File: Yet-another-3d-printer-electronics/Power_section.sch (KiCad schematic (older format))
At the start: 33 parts, among them U7 AOZ1284PI, U8 AOZ1284PI

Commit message: Replace aoz1284pi by AP1501
Signed-off-by: Mateusz Krawczuk <mat.krawczuk@gmail.com>
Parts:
- removed C17, C18, C19, C20, C21, C22, C? (x3): C, symbol C
- removed D43, D44, D?: D_Schottky, symbol D_Schottky
- removed L2, L3, L?: INDUCTOR, symbol INDUCTOR
- removed R24, R25, R26, R27, R28, R29, R? (x6), RC1, RC2, RC?: R, symbol R
- removed U7, U8, U?: AOZ1284PI, symbol AOZ1284PI
- added C? (x6): CP, symbol CP
- added D? (x3): D_Schottky, symbol D_Schottky
- added L? (x3): L, symbol L
- added R? (x6): R, symbol R
- added U? (x3): AP1501, symbol AP1501
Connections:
- wire segments 81 -> 48

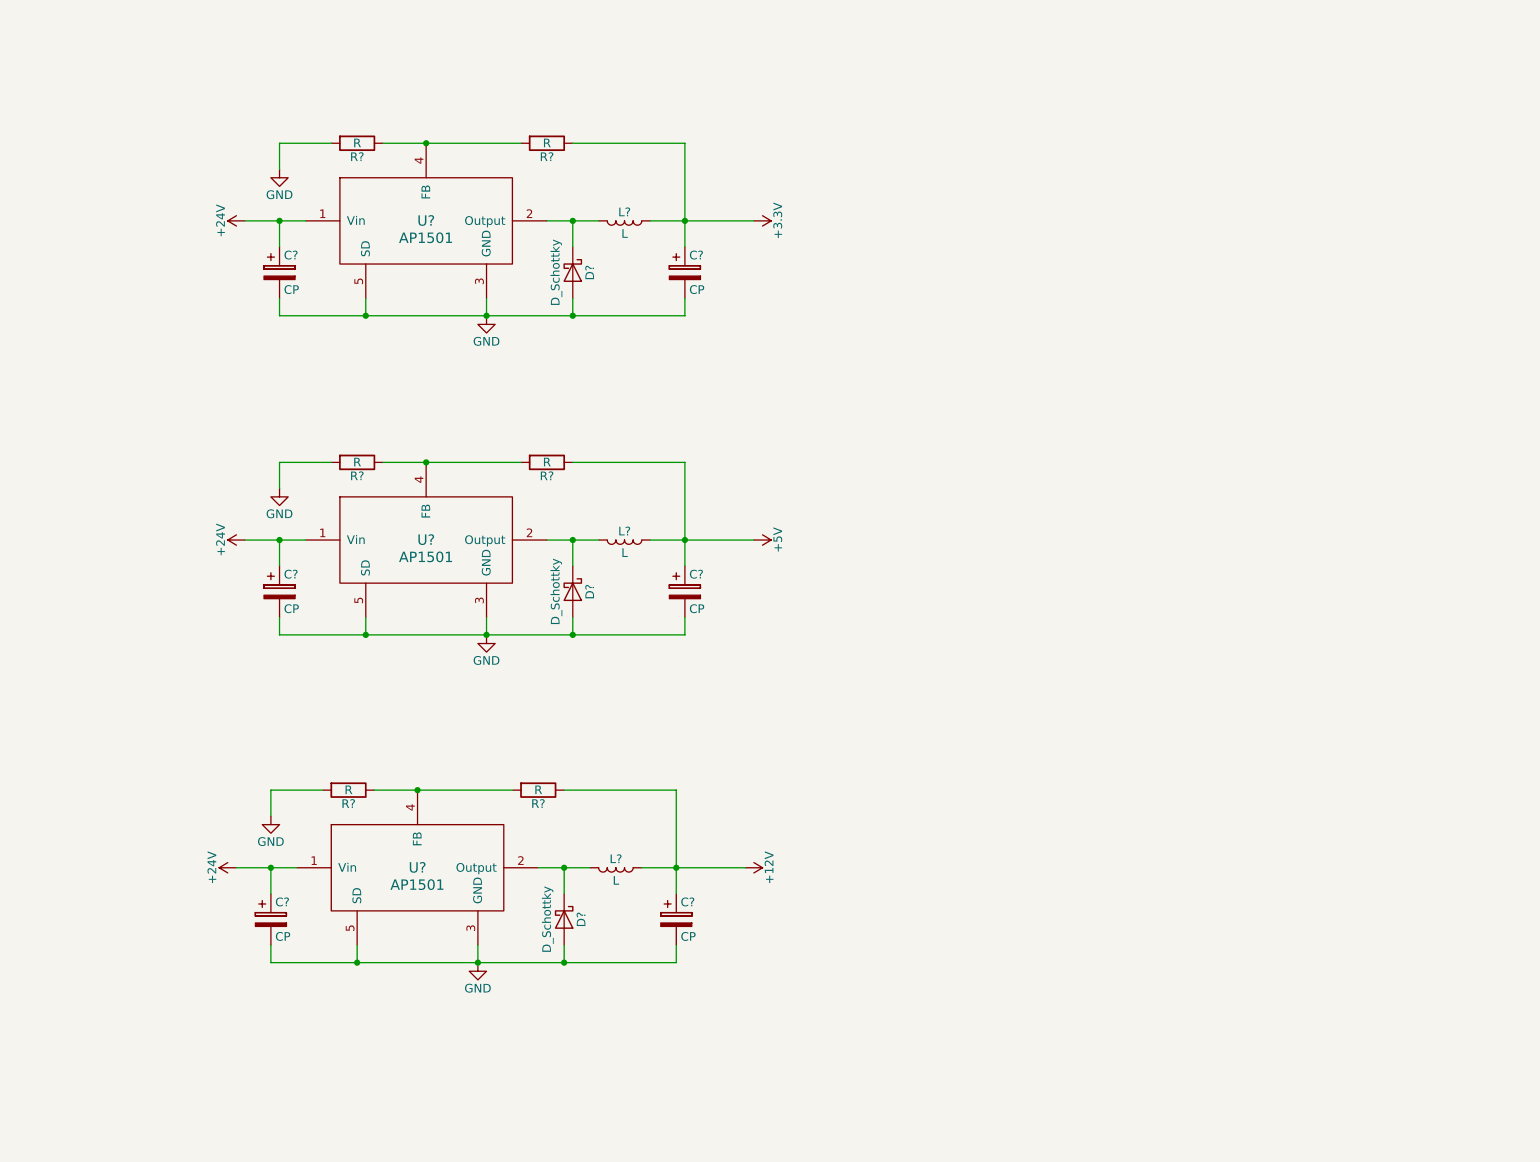
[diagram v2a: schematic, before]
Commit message: Add additional stepstick, hotend fan and heater and temperature sensor
Extruder stepsticks have independ enables pins. Vcc was replace by valid
power source.

Signed-off-by: Mateusz Krawczuk <mat.krawczuk@gmail.com>
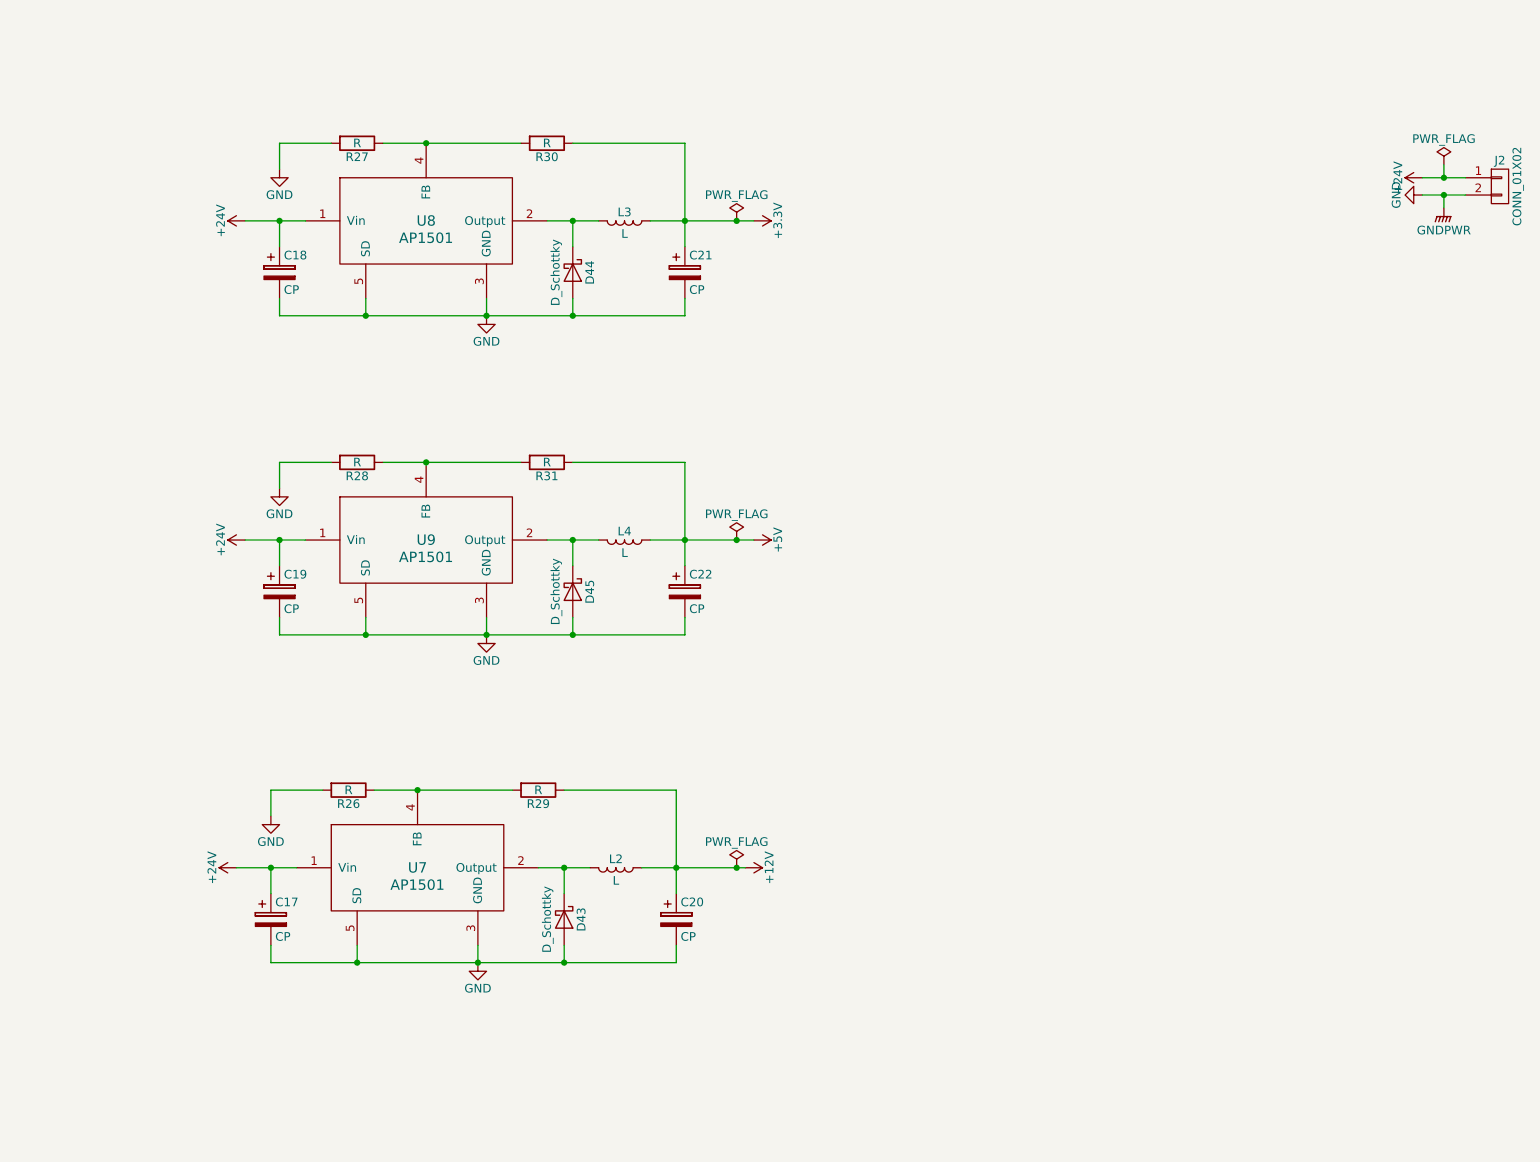
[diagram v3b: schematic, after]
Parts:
- added J2: CONN_01X02, symbol CONN_01X02
- gave numbers to parts that had none: 21
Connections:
- net +24V: now also J2.1 (P1)
- net GND: now also J2.2 (P2)

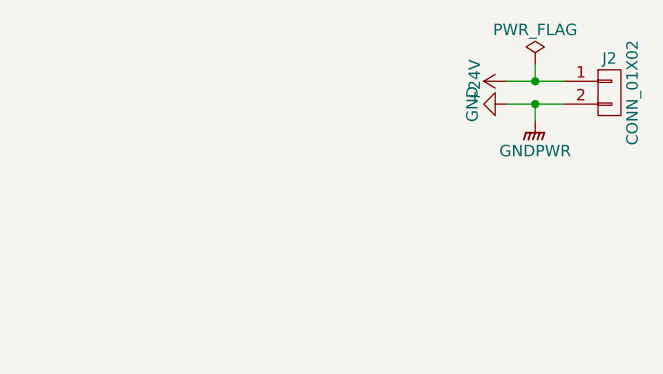
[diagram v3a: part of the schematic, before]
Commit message: Add fuses to powersupply connector and heatbed.
TVS diode used to protect pins from short circuit. Correct connectors
names.

Signed-off-by: Mateusz Krawczuk <mat.krawczuk@gmail.com>
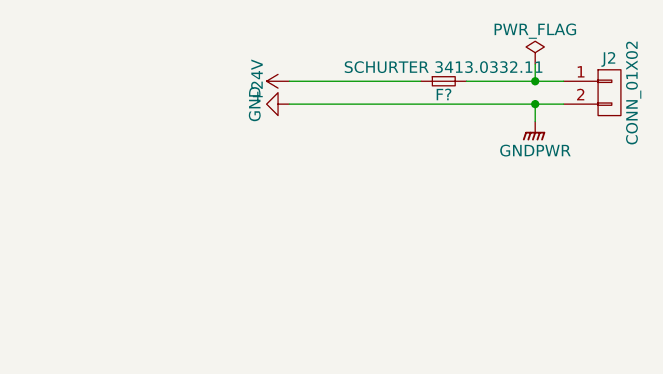
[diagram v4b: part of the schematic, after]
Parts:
- added F?: SCHURTER 3413.0332.11, symbol Fuse_Small
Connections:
- net +24V: now also F?.1; no longer J2.1 (P1)
- new net: F?.2, J2.1 (P1)
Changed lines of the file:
@@
 L +24V #PWR094
 U 1 1 58FF7D10
-P 8975 1650
-F 0 "#PWR094" H 8975 1500 50  0001 C CNN
-F 1 "+24V" H 8975 1790 50  0000 C CNN
-F 2 "" H 8975 1650 50  0001 C CNN
-F 3 "" H 8975 1650 50  0001 C CNN
-	1    8975 1650
+P 8025 1650
+F 0 "#PWR094" H 8025 1500 50  0001 C CNN
+F 1 "+24V" H 8025 1790 50  0000 C CNN
+F 2 "" H 8025 1650 50  0001 C CNN
+F 3 "" H 8025 1650 50  0001 C CNN
+	1    8025 1650
 	0    -1   -1   0
 $EndComp
 Wire Wire Line
-	8975 1650 9225 1650
+	8800 1650 9225 1650
 $Comp
 L PWR_FLAG #FLG095
@@
 L GND #PWR096
 U 1 1 58FF7FE9
-P 8975 1750
-F 0 "#PWR096" H 8975 1500 50  0001 C CNN
-F 1 "GND" H 8975 1600 50  0000 C CNN
-F 2 "" H 8975 1750 50  0001 C CNN
-F 3 "" H 8975 1750 50  0001 C CNN
-	1    8975 1750
+P 8025 1750
+F 0 "#PWR096" H 8025 1500 50  0001 C CNN
+F 1 "GND" H 8025 1600 50  0000 C CNN
+F 2 "" H 8025 1750 50  0001 C CNN
+F 3 "" H 8025 1750 50  0001 C CNN
+	1    8025 1750
 	0    1    1    0
 $EndComp
 Wire Wire Line
-	8975 1750 9225 1750
+	8025 1750 9225 1750
 $Comp
 L GNDPWR #PWR097
@@
 Connection ~ 5000 3750
 Connection ~ 5000 1900
+$Comp
+L Fuse_Small F?
+U 1 1 590414B9
+P 8700 1650
+F 0 "F?" H 8700 1590 50  0000 C CNN
+F 1 "SCHURTER 3413.0332.11" H 8700 1710 50  0000 C CNN
+F 2 "" H 8700 1650 50  0001 C CNN
+F 3 "" H 8700 1650 50  0001 C CNN
+	1    8700 1650
+	1    0    0    -1
+$EndComp
+Wire Wire Line
+	8600 1650 8025 1650
 $EndSCHEMATC

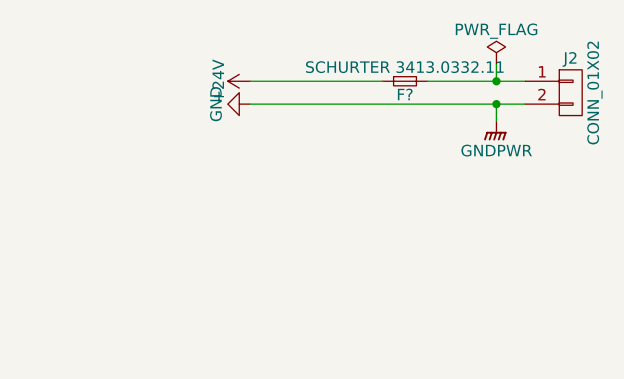
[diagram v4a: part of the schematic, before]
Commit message: Add programming jumper
Signed-off-by: Mateusz Krawczuk <mat.krawczuk@gmail.com>
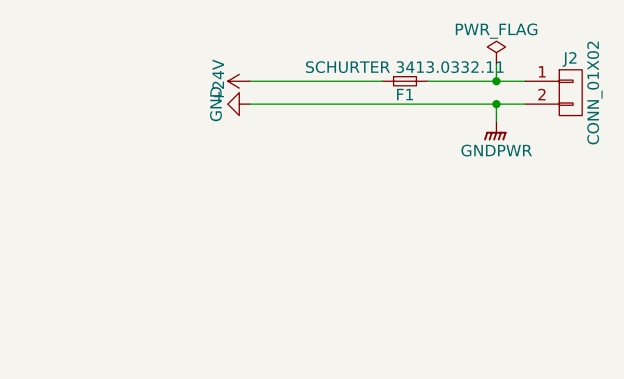
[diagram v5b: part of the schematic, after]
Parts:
- gave numbers to parts that had none: 1
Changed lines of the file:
@@
 $EndDescr
 $Comp
-L +24V #PWR082
+L +24V #PWR83
 U 1 1 58B11BCF
 P 2150 1900
-F 0 "#PWR082" H 2150 1750 50  0001 C CNN
+F 0 "#PWR83" H 2150 1750 50  0001 C CNN
 F 1 "+24V" H 2150 2040 50  0000 C CNN
 F 2 "" H 2150 1900 50  0000 C CNN
@@
 Connection ~ 4700 1900
 $Comp
-L +3.3V #PWR083
+L +3.3V #PWR92
 U 1 1 58FD74DD
 P 5100 1900
-F 0 "#PWR083" H 5100 1750 50  0001 C CNN
+F 0 "#PWR92" H 5100 1750 50  0001 C CNN
 F 1 "+3.3V" H 5100 2040 50  0000 C CNN
 F 2 "" H 5100 1900 50  0001 C CNN
@@
 $EndComp
 $Comp
-L GND #PWR084
+L GND #PWR89
 U 1 1 58FD7722
 P 3550 2450
-F 0 "#PWR084" H 3550 2200 50  0001 C CNN
+F 0 "#PWR89" H 3550 2200 50  0001 C CNN
 F 1 "GND" H 3550 2300 50  0000 C CNN
 F 2 "" H 3550 2450 50  0001 C CNN
@@
 $EndComp
 $Comp
-L GND #PWR085
+L GND #PWR86
 U 1 1 58FD7743
 P 2350 1600
-F 0 "#PWR085" H 2350 1350 50  0001 C CNN
+F 0 "#PWR86" H 2350 1350 50  0001 C CNN
 F 1 "GND" H 2350 1450 50  0000 C CNN
 F 2 "" H 2350 1600 50  0001 C CNN
@@
 	4050 2350 4050 2450
 $Comp
-L +24V #PWR086
+L +24V #PWR84
 U 1 1 58FD7B9F
 P 2150 3750
-F 0 "#PWR086" H 2150 3600 50  0001 C CNN
+F 0 "#PWR84" H 2150 3600 50  0001 C CNN
 F 1 "+24V" H 2150 3890 50  0000 C CNN
 F 2 "" H 2150 3750 50  0000 C CNN
@@
 Connection ~ 4700 3750
 $Comp
-L GND #PWR087
+L GND #PWR90
 U 1 1 58FD7BD8
 P 3550 4300
-F 0 "#PWR087" H 3550 4050 50  0001 C CNN
+F 0 "#PWR90" H 3550 4050 50  0001 C CNN
 F 1 "GND" H 3550 4150 50  0000 C CNN
 F 2 "" H 3550 4300 50  0001 C CNN
@@
 $EndComp
 $Comp
-L GND #PWR088
+L GND #PWR87
 U 1 1 58FD7BDE
 P 2350 3450
-F 0 "#PWR088" H 2350 3200 50  0001 C CNN
+F 0 "#PWR87" H 2350 3200 50  0001 C CNN
 F 1 "GND" H 2350 3300 50  0000 C CNN
 F 2 "" H 2350 3450 50  0001 C CNN
@@
 	4050 4200 4050 4300
 $Comp
-L +24V #PWR089
+L +24V #PWR82
 U 1 1 58FD7F6A
 P 2100 5650
-F 0 "#PWR089" H 2100 5500 50  0001 C CNN
+F 0 "#PWR82" H 2100 5500 50  0001 C CNN
 F 1 "+24V" H 2100 5790 50  0000 C CNN
 F 2 "" H 2100 5650 50  0000 C CNN
@@
 Connection ~ 4650 5650
 $Comp
-L GND #PWR090
+L GND #PWR88
 U 1 1 58FD7FA3
 P 3500 6200
-F 0 "#PWR090" H 3500 5950 50  0001 C CNN
+F 0 "#PWR88" H 3500 5950 50  0001 C CNN
 F 1 "GND" H 3500 6050 50  0000 C CNN
 F 2 "" H 3500 6200 50  0001 C CNN
@@
 $EndComp
 $Comp
-L GND #PWR091
+L GND #PWR85
 U 1 1 58FD7FA9
 P 2300 5350
-F 0 "#PWR091" H 2300 5100 50  0001 C CNN
+F 0 "#PWR85" H 2300 5100 50  0001 C CNN
 F 1 "GND" H 2300 5200 50  0000 C CNN
 F 2 "" H 2300 5350 50  0001 C CNN
@@
 	4000 6100 4000 6200
 $Comp
-L +5V #PWR092
+L +5V #PWR93
 U 1 1 58FD8102
 P 5100 3750
-F 0 "#PWR092" H 5100 3600 50  0001 C CNN
+F 0 "#PWR93" H 5100 3600 50  0001 C CNN
 F 1 "+5V" H 5100 3890 50  0000 C CNN
 F 2 "" H 5100 3750 50  0001 C CNN
@@
 $EndComp
 $Comp
-L +12V #PWR093
+L +12V #PWR91
 U 1 1 58FD82BA
 P 5050 5650
-F 0 "#PWR093" H 5050 5500 50  0001 C CNN
+F 0 "#PWR91" H 5050 5500 50  0001 C CNN
 F 1 "+12V" H 5050 5790 50  0000 C CNN
 F 2 "" H 5050 5650 50  0001 C CNN
@@
 $EndComp
 $Comp
-L +24V #PWR094
+L +24V #PWR94
 U 1 1 58FF7D10
 P 8025 1650
-F 0 "#PWR094" H 8025 1500 50  0001 C CNN
+F 0 "#PWR94" H 8025 1500 50  0001 C CNN
 F 1 "+24V" H 8025 1790 50  0000 C CNN
 F 2 "" H 8025 1650 50  0001 C CNN
@@
 	8800 1650 9225 1650
 $Comp
-L PWR_FLAG #FLG095
+L PWR_FLAG #FLG5
 U 1 1 58FF7EEB
 P 9100 1575
-F 0 "#FLG095" H 9100 1650 50  0001 C CNN
+F 0 "#FLG5" H 9100 1650 50  0001 C CNN
 F 1 "PWR_FLAG" H 9100 1725 50  0000 C CNN
 F 2 "" H 9100 1575 50  0001 C CNN
@@
 Connection ~ 9100 1650
 $Comp
-L GND #PWR096
+L GND #PWR95
 U 1 1 58FF7FE9
 P 8025 1750
-F 0 "#PWR096" H 8025 1500 50  0001 C CNN
+F 0 "#PWR95" H 8025 1500 50  0001 C CNN
 F 1 "GND" H 8025 1600 50  0000 C CNN
 F 2 "" H 8025 1750 50  0001 C CNN
@@
 	8025 1750 9225 1750
 $Comp
-L GNDPWR #PWR097
+L GNDPWR #PWR96
 U 1 1 58FF8089
 P 9100 1825
-F 0 "#PWR097" H 9100 1625 50  0001 C CNN
+F 0 "#PWR96" H 9100 1625 50  0001 C CNN
 F 1 "GNDPWR" H 9100 1695 50  0000 C CNN
 F 2 "" H 9100 1775 50  0001 C CNN
@@
 Connection ~ 9100 1750
 $Comp
-L PWR_FLAG #FLG098
+L PWR_FLAG #FLG3
 U 1 1 59003F28
 P 5000 3750
-F 0 "#FLG098" H 5000 3825 50  0001 C CNN
+F 0 "#FLG3" H 5000 3825 50  0001 C CNN
 F 1 "PWR_FLAG" H 5000 3900 50  0000 C CNN
 F 2 "" H 5000 3750 50  0001 C CNN
@@
 $EndComp
 $Comp
-L PWR_FLAG #FLG099
+L PWR_FLAG #FLG2
 U 1 1 59003F75
 P 5000 1900
-F 0 "#FLG099" H 5000 1975 50  0001 C CNN
+F 0 "#FLG2" H 5000 1975 50  0001 C CNN
 F 1 "PWR_FLAG" H 5000 2050 50  0000 C CNN
 F 2 "" H 5000 1900 50  0001 C CNN
@@
 $EndComp
 $Comp
-L PWR_FLAG #FLG0100
+L PWR_FLAG #FLG4
 U 1 1 590042F0
 P 5000 5650
-F 0 "#FLG0100" H 5000 5725 50  0001 C CNN
+F 0 "#FLG4" H 5000 5725 50  0001 C CNN
 F 1 "PWR_FLAG" H 5000 5800 50  0000 C CNN
 F 2 "" H 5000 5650 50  0001 C CNN
@@
 Connection ~ 5000 1900
 $Comp
-L Fuse_Small F?
+L Fuse_Small F1
 U 1 1 590414B9
 P 8700 1650
-F 0 "F?" H 8700 1590 50  0000 C CNN
+F 0 "F1" H 8700 1590 50  0000 C CNN
 F 1 "SCHURTER 3413.0332.11" H 8700 1710 50  0000 C CNN
 F 2 "" H 8700 1650 50  0001 C CNN
